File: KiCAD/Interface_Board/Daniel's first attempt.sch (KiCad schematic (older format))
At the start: 36 parts, among them J1 TB001-500-04BE, J2 Conn_02x15_Top_Bottom

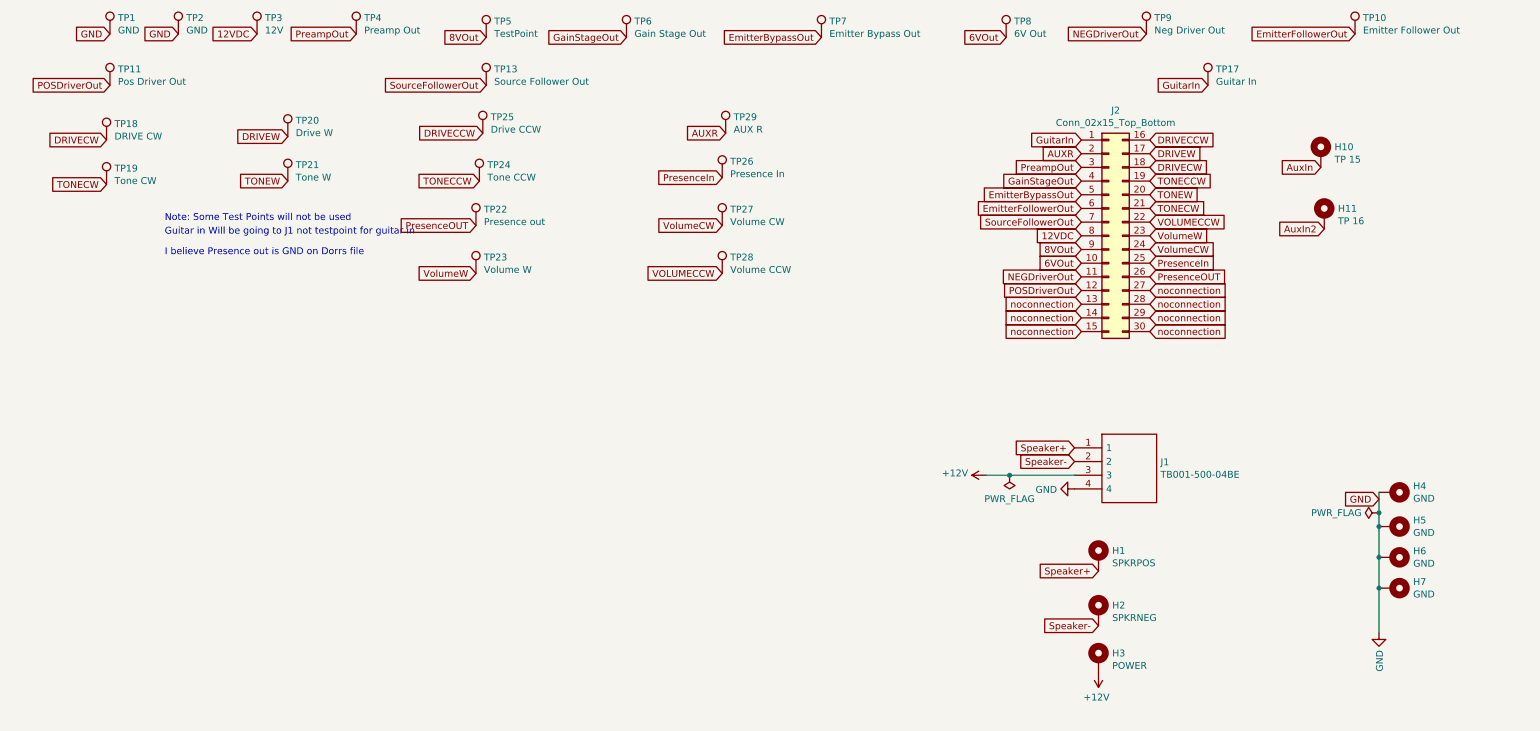
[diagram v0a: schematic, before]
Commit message: Reminder: Need to change diameter of TP points from 2.0mm to 1.75mm before sign off
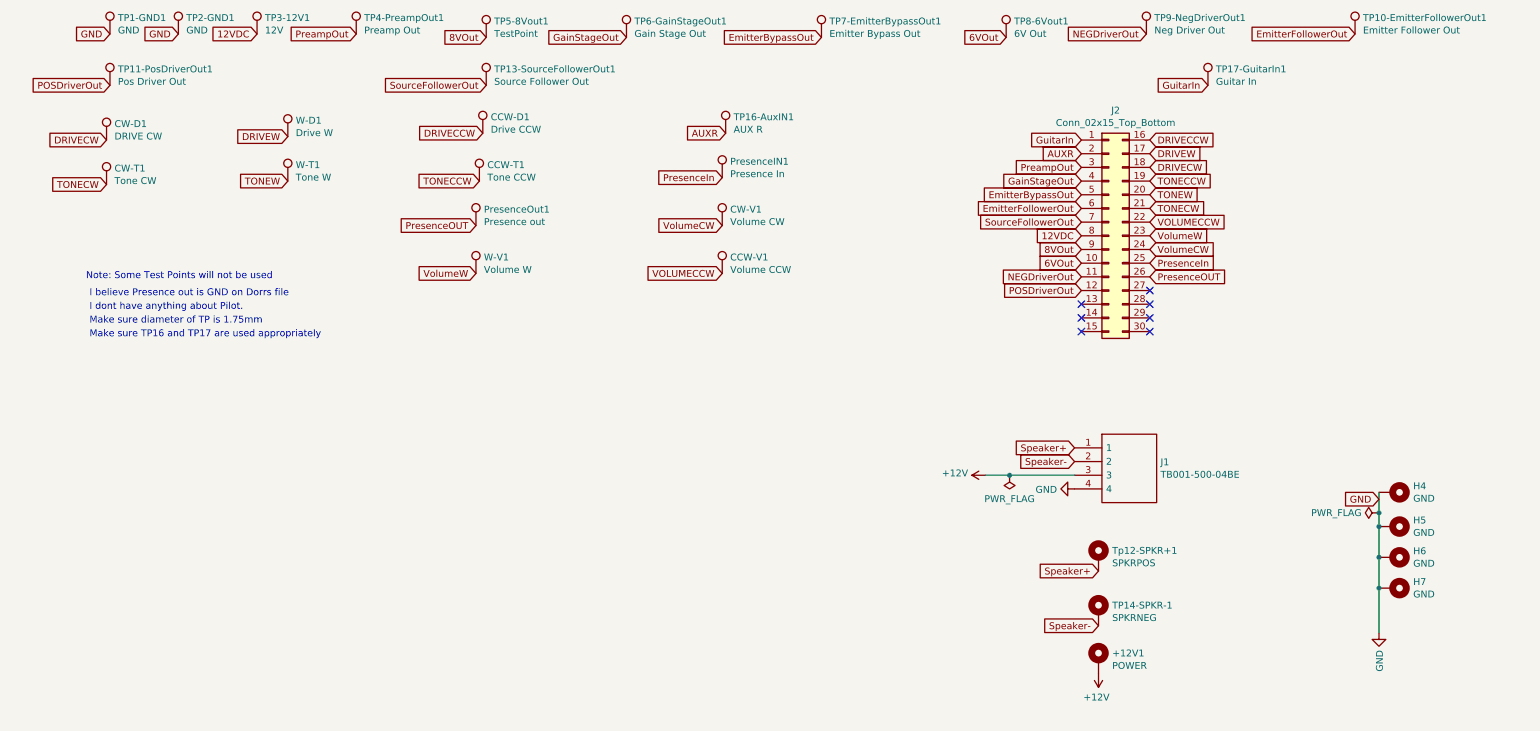
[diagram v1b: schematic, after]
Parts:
- removed H10: TP 15, TestPoint:TestPoint_Plated_Hole_D2.0mm, symbol Mechanical:MountingHole_Pad
- removed H11: TP 16, TestPoint:TestPoint_Plated_Hole_D2.0mm, symbol Mechanical:MountingHole_Pad
- renumbered H3 to +12V1, TP25 to CCW-D1, TP24 to CCW-T1, TP28 to CCW-V1, TP18 to CW-D1, TP19 to CW-T1, TP27 to CW-V1, TP26 to PresenceIN1, TP22 to PresenceOut1, TP1 to TP1-GND1, TP10 to TP10-EmitterFollowerOut1, TP11 to TP11-PosDriverOut1, TP13 to TP13-SourceFollowerOut1, H2 to TP14-SPKR-1, TP29 to TP16-AuxIN1, TP17 to TP17-GuitarIn1, TP2 to TP2-GND1, TP3 to TP3-12V1, TP4 to TP4-PreampOut1, TP5 to TP5-8Vout1, TP6 to TP6-GainStageOut1, TP7 to TP7-EmitterBypassOut1, TP8 to TP8-6Vout1, TP9 to TP9-NegDriverOut1, H1 to Tp12-SPKR+1, TP20 to W-D1, TP21 to W-T1, TP23 to W-V1
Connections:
- removed net noconnection: J2.13 (Pin_13), J2.14 (Pin_14), J2.15 (Pin_15), J2.27 (Pin_27), J2.28 (Pin_28), J2.29 (Pin_29), J2.30 (Pin_30)
- no-connect marks 0 -> 7
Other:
- note added: "I dont have anything about Pilot."
- note added: "Make sure TP16 and TP17 are used appropriately"
- note added: "Make sure diameter of TP is 1.75mm"
- note removed: "Guitar in Will be going to J1 not testpoint for guitar in"

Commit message: Zero Vias needed :)!! added vias only for GND if necessary. Note: Since we are plugging in the cable to the bottom of the testboard, the ribbon cable will be flipped therefore, the test points on the ribbon will be flipped. I swapped the couples for each row accordingly. So far if we get the green light from Mark, This baby will be read to show tomorrow to Professor Dorr.
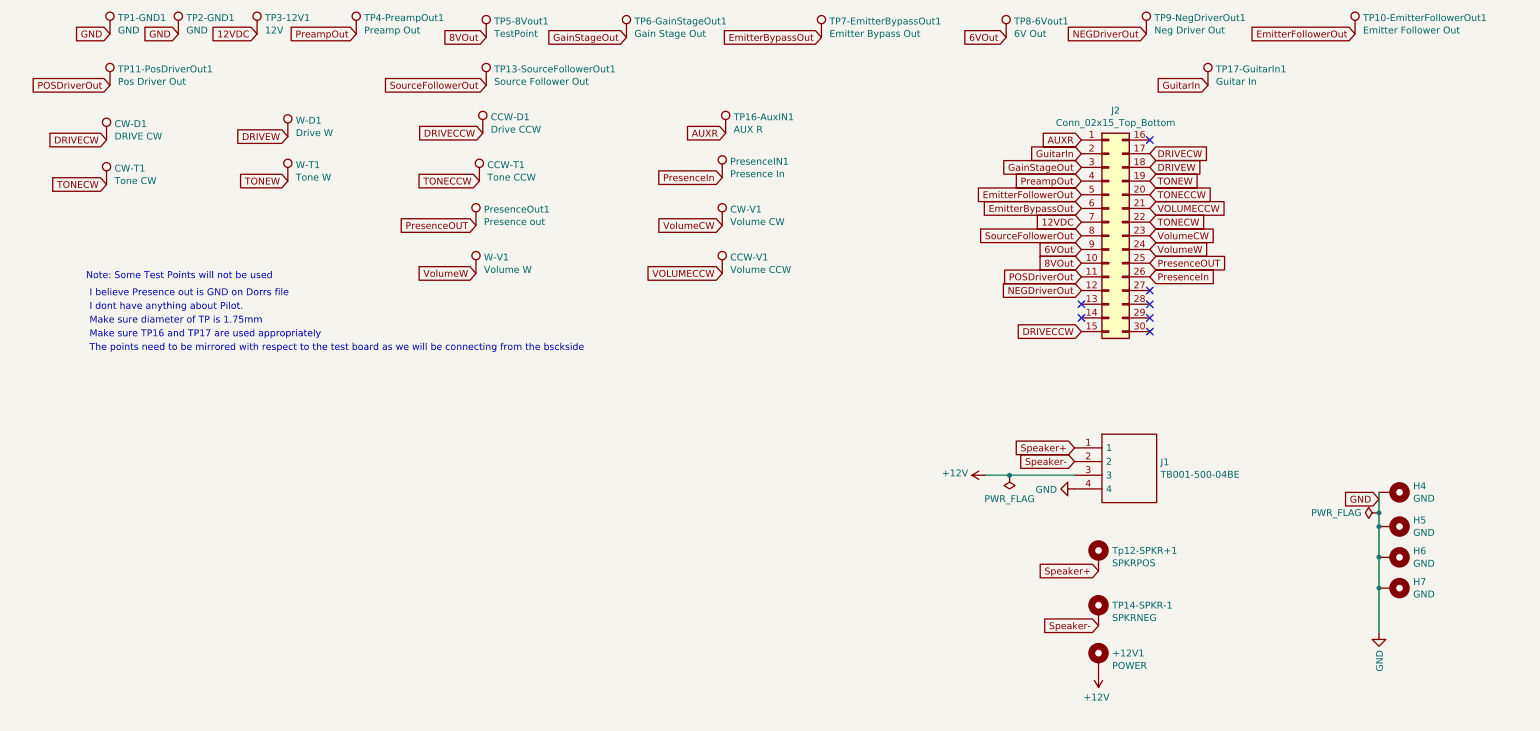
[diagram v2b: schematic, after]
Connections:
- net 12VDC: now also J2.7 (Pin_7); no longer J2.8 (Pin_8)
- net 6VOut: now also J2.9 (Pin_9); no longer J2.10 (Pin_10)
- net 8VOut: now also J2.10 (Pin_10); no longer J2.9 (Pin_9)
- net AUXR: now also J2.1 (Pin_1); no longer J2.2 (Pin_2)
- net DRIVECCW: now also J2.15 (Pin_15); no longer J2.16 (Pin_16)
- net DRIVECW: now also J2.17 (Pin_17); no longer J2.18 (Pin_18)
- net DRIVEW: now also J2.18 (Pin_18); no longer J2.17 (Pin_17)
- net EmitterBypassOut: now also J2.6 (Pin_6); no longer J2.5 (Pin_5)
- net EmitterFollowerOut: now also J2.5 (Pin_5); no longer J2.6 (Pin_6)
- net GainStageOut: now also J2.3 (Pin_3); no longer J2.4 (Pin_4)
- net GuitarIn: now also J2.2 (Pin_2); no longer J2.1 (Pin_1)
- net NEGDriverOut: now also J2.12 (Pin_12); no longer J2.11 (Pin_11)
- net POSDriverOut: now also J2.11 (Pin_11); no longer J2.12 (Pin_12)
- net PreampOut: now also J2.4 (Pin_4); no longer J2.3 (Pin_3)
- net PresenceIn: now also J2.26 (Pin_26); no longer J2.25 (Pin_25)
- net PresenceOUT: now also J2.25 (Pin_25); no longer J2.26 (Pin_26)
- net SourceFollowerOut: now also J2.8 (Pin_8); no longer J2.7 (Pin_7)
- net TONECCW: now also J2.20 (Pin_20); no longer J2.19 (Pin_19)
- net TONECW: now also J2.22 (Pin_22); no longer J2.21 (Pin_21)
- net TONEW: now also J2.19 (Pin_19); no longer J2.20 (Pin_20)
- net VOLUMECCW: now also J2.21 (Pin_21); no longer J2.22 (Pin_22)
- net VolumeCW: now also J2.23 (Pin_23); no longer J2.24 (Pin_24)
- net VolumeW: now also J2.24 (Pin_24); no longer J2.23 (Pin_23)
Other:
- note added: "The points need to be mirrored with respect to the test board as we will be connecting from the bsckside"
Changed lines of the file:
@@
 Text GLabel 2350 1250 0    50   Input ~ 0
 12VDC
-Text GLabel 8375 2725 0    50   Input ~ 0
+Text GLabel 8375 2625 0    50   Input ~ 0
 12VDC
 $Comp
@@
 Text GLabel 3075 1250 0    50   Input ~ 0
 PreampOut
-Text GLabel 8375 2225 0    50   Input ~ 0
+Text GLabel 8375 2325 0    50   Input ~ 0
 PreampOut
 Text GLabel 5050 1275 0    50   Input ~ 0
 GainStageOut
-Text GLabel 8375 2325 0    50   Input ~ 0
+Text GLabel 8375 2225 0    50   Input ~ 0
 GainStageOut
 Text GLabel 6475 1275 0    50   Input ~ 0
 EmitterBypassOut
-Text GLabel 8375 2425 0    50   Input ~ 0
+Text GLabel 8375 2525 0    50   Input ~ 0
 EmitterBypassOut
 Text GLabel 7825 1275 0    50   Input ~ 0
 6VOut
-Text GLabel 8375 2925 0    50   Input ~ 0
+Text GLabel 8375 2825 0    50   Input ~ 0
 6VOut
 Text GLabel 8850 1250 0    50   Input ~ 0
 NEGDriverOut
-Text GLabel 8375 3025 0    50   Input ~ 0
+Text GLabel 8375 3125 0    50   Input ~ 0
 NEGDriverOut
-Text GLabel 8375 2525 0    50   Input ~ 0
+Text GLabel 8375 2425 0    50   Input ~ 0
 EmitterFollowerOut
 Text GLabel 1275 1625 0    50   Input ~ 0
 POSDriverOut
-Text GLabel 8375 3125 0    50   Input ~ 0
+Text GLabel 8375 3025 0    50   Input ~ 0
 POSDriverOut
 Text GLabel 4025 1625 0    50   Input ~ 0
 SourceFollowerOut
-Text GLabel 8375 2625 0    50   Input ~ 0
+Text GLabel 8375 2725 0    50   Input ~ 0
 SourceFollowerOut
 Text GLabel 9300 1625 0    50   Input ~ 0
 GuitarIn
-Text GLabel 8375 2025 0    50   Input ~ 0
+Text GLabel 8375 2125 0    50   Input ~ 0
 GuitarIn
 Text GLabel 4025 1275 0    50   Input ~ 0
 8VOut
-Text GLabel 8375 2825 0    50   Input ~ 0
+Text GLabel 8375 2925 0    50   Input ~ 0
 8VOut
 Text Notes 1100 3050 0    50   ~ 0
@@
 Text GLabel 3950 3000 0    50   Input ~ 0
 VolumeW
-Text GLabel 8875 2025 2    50   Input ~ 0
-DRIVECCW
-Text GLabel 8875 2125 2    50   Input ~ 0
-DRIVEW
 Text GLabel 1250 2025 0    50   Input ~ 0
 DRIVECW
-Text GLabel 8875 2225 2    50   Input ~ 0
+Text GLabel 8875 2125 2    50   Input ~ 0
 DRIVECW
+Text GLabel 8875 2425 2    50   Input ~ 0
+TONECCW
 Text GLabel 8875 2325 2    50   Input ~ 0
-TONECCW
-Text GLabel 8875 2425 2    50   Input ~ 0
 TONEW
-Text GLabel 8875 2525 2    50   Input ~ 0
+Text GLabel 8875 2625 2    50   Input ~ 0
 TONECW
-Text GLabel 8875 2825 2    50   Input ~ 0
+Text GLabel 8875 2725 2    50   Input ~ 0
 VolumeCW
 Text GLabel 5750 3000 0    50   Input ~ 0
 VOLUMECCW
-Text GLabel 8875 2625 2    50   Input ~ 0
+Text GLabel 8875 2525 2    50   Input ~ 0
 VOLUMECCW
-Text GLabel 8875 2725 2    50   Input ~ 0
+Text GLabel 8875 2825 2    50   Input ~ 0
 VolumeW
+Text GLabel 8875 3025 2    50   Input ~ 0
+PresenceIn
 Text GLabel 8875 2925 2    50   Input ~ 0
-PresenceIn
-Text GLabel 8875 3025 2    50   Input ~ 0
 PresenceOUT
 Text GLabel 10375 1250 0    50   Input ~ 0
 EmitterFollowerOut
-Text GLabel 8375 2125 0    50   Input ~ 0
+Text GLabel 8375 2025 0    50   Input ~ 0
 AUXR
 Text Notes 1125 3275 0    50   ~ 0
@@
 NoConn ~ 8875 3325
 NoConn ~ 8875 3425
-NoConn ~ 8375 3425
+NoConn ~ 8875 2025
 NoConn ~ 8375 3325
 NoConn ~ 8375 3225
+Text Notes 1125 3575 0    50   ~ 0
+The points need to be mirrored with respect to the test board as we will be connecting from the bsckside
+Text GLabel 8875 2225 2    50   Input ~ 0
+DRIVEW
+Text GLabel 8375 3425 0    50   Input ~ 0
+DRIVECCW
 $EndSCHEMATC

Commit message: Final Rev 1. Sent To mark to mil, hopefully have before End of Day
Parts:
- added GNDP1: GND, TestPoint:TestPoint_Plated_Hole_D2.0mm, symbol Mechanical:MountingHole_Pad
- H4, H5, H6, H7: footprint MountingHole:MountingHole_3.2mm_M3_Pad_Via -> MountingHole:MountingHole_3.7mm_Pad_Via
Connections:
- net GND: now also GNDP1.1
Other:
- moved on the sheet: +12V1
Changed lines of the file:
@@
 F 0 "H6" V 10604 5225 50  0000 L CNN
 F 1 "GND" V 10695 5225 50  0000 L CNN
-F 2 "MountingHole:MountingHole_3.2mm_M3_Pad_Via" H 10650 5075 50  0001 C CNN
+F 2 "MountingHole:MountingHole_3.7mm_Pad_Via" H 10650 5075 50  0001 C CNN
 F 3 "~" H 10650 5075 50  0001 C CNN
 	1    10650 5075
@@
 F 0 "H7" V 10604 5450 50  0000 L CNN
 F 1 "GND" V 10695 5450 50  0000 L CNN
-F 2 "MountingHole:MountingHole_3.2mm_M3_Pad_Via" H 10650 5300 50  0001 C CNN
+F 2 "MountingHole:MountingHole_3.7mm_Pad_Via" H 10650 5300 50  0001 C CNN
 F 3 "~" H 10650 5300 50  0001 C CNN
 	1    10650 5300
@@
 F 0 "H5" V 10604 5000 50  0000 L CNN
 F 1 "GND" V 10695 5000 50  0000 L CNN
-F 2 "MountingHole:MountingHole_3.2mm_M3_Pad_Via" H 10650 4850 50  0001 C CNN
+F 2 "MountingHole:MountingHole_3.7mm_Pad_Via" H 10650 4850 50  0001 C CNN
 F 3 "~" H 10650 4850 50  0001 C CNN
 	1    10650 4850
@@
 F 0 "H4" V 10604 4750 50  0000 L CNN
 F 1 "GND" V 10695 4750 50  0000 L CNN
-F 2 "MountingHole:MountingHole_3.2mm_M3_Pad_Via" H 10650 4600 50  0001 C CNN
+F 2 "MountingHole:MountingHole_3.7mm_Pad_Via" H 10650 4600 50  0001 C CNN
 F 3 "~" H 10650 4600 50  0001 C CNN
 	1    10650 4600
@@
 L Mechanical:MountingHole_Pad +12V1
 U 1 1 617FC400
-P 8500 5825
-F 0 "+12V1" H 8600 5874 50  0000 L CNN
-F 1 "POWER" H 8600 5783 50  0000 L CNN
-F 2 "TestPoint:TestPoint_Plated_Hole_D2.0mm" H 8500 5825 50  0001 C CNN
-F 3 "~" H 8500 5825 50  0001 C CNN
-	1    8500 5825
+P 8500 5850
+F 0 "+12V1" H 8600 5899 50  0000 L CNN
+F 1 "POWER" H 8600 5808 50  0000 L CNN
+F 2 "TestPoint:TestPoint_Plated_Hole_D2.0mm" H 8500 5850 50  0001 C CNN
+F 3 "~" H 8500 5850 50  0001 C CNN
+	1    8500 5850
 	1    0    0    -1
 $EndComp
@@
 L power:+12V #PWR03
 U 1 1 617F42E2
-P 8500 5925
-F 0 "#PWR03" H 8500 5775 50  0001 C CNN
-F 1 "+12V" H 8515 6098 50  0000 C CNN
-F 2 "" H 8500 5925 50  0001 C CNN
-F 3 "" H 8500 5925 50  0001 C CNN
-	1    8500 5925
+P 8500 5950
+F 0 "#PWR03" H 8500 5800 50  0001 C CNN
+F 1 "+12V" H 8515 6123 50  0000 C CNN
+F 2 "" H 8500 5950 50  0001 C CNN
+F 3 "" H 8500 5950 50  0001 C CNN
+	1    8500 5950
 	-1   0    0    1
 $EndComp
@@
 Text GLabel 8375 3425 0    50   Input ~ 0
 DRIVECCW
+$Comp
+L Mechanical:MountingHole_Pad GNDP1
+U 1 1 6185C568
+P 9225 5850
+F 0 "GNDP1" H 9325 5899 50  0000 L CNN
+F 1 "GND" H 9325 5808 50  0000 L CNN
+F 2 "TestPoint:TestPoint_Plated_Hole_D2.0mm" H 9225 5850 50  0001 C CNN
+F 3 "~" H 9225 5850 50  0001 C CNN
+	1    9225 5850
+	1    0    0    -1
+$EndComp
+$Comp
+L power:GND #PWR05
+U 1 1 6185C899
+P 9225 5950
+F 0 "#PWR05" H 9225 5700 50  0001 C CNN
+F 1 "GND" V 9230 5822 50  0000 R CNN
+F 2 "" H 9225 5950 50  0001 C CNN
+F 3 "" H 9225 5950 50  0001 C CNN
+	1    9225 5950
+	1    0    0    -1
+$EndComp
 $EndSCHEMATC
